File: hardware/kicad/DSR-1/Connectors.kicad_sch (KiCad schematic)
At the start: 0 parts

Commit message: Completed microcontroller schematic
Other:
- title: (none) -> Connectors
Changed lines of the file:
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@@
 	(generator_version "10.0")
 	(paper "A4")
+	(title_block
+		(title "Connectors")
+		(date "2026-05-31")
+		(rev "1")
+	)
 	(hierarchical_label "SPEED_TUNE_SW"
 		(shape output)

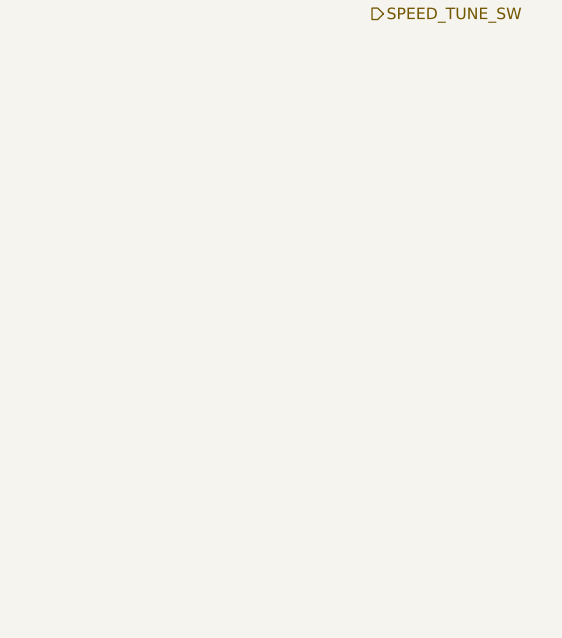
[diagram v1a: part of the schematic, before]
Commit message: completed schematics through sheet 5.
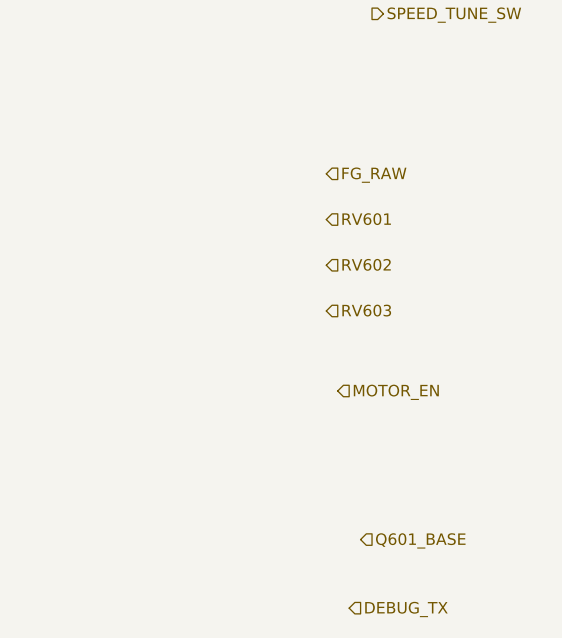
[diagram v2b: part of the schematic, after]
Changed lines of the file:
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@@
 		(rev "1")
+	)
+	(hierarchical_label "DEBUG_TX"
+		(shape input)
+		(at 262.89 99.06 0)
+		(effects
+			(font
+				(size 1.27 1.27)
+			)
+			(justify left)
+		)
 	)
 	(hierarchical_label "SPEED_TUNE_SW"
@@
 		)
 	)
+	(hierarchical_label "MOTOR_EN"
+		(shape input)
+		(at 261.62 74.93 0)
+		(effects
+			(font
+				(size 1.27 1.27)
+			)
+			(justify left)
+		)
+	)
+	(hierarchical_label "RV603"
+		(shape input)
+		(at 260.35 66.04 0)
+		(effects
+			(font
+				(size 1.27 1.27)
+			)
+			(justify left)
+		)
+	)
+	(hierarchical_label "RV601"
+		(shape input)
+		(at 260.35 55.88 0)
+		(effects
+			(font
+				(size 1.27 1.27)
+			)
+			(justify left)
+		)
+	)
+	(hierarchical_label "RV602"
+		(shape input)
+		(at 260.35 60.96 0)
+		(effects
+			(font
+				(size 1.27 1.27)
+			)
+			(justify left)
+		)
+	)
 	(hierarchical_label "SWDIO"
 		(shape output)
@@
 		(effects
 			(font
+				(size 1.27 1.27)
+			)
+			(justify left)
+		)
+	)
+	(hierarchical_label "Q601_BASE"
+		(shape input)
+		(at 264.16 91.44 0)
+		(effects
+			(font
+				(size 1.27 1.27)
+			)
+			(justify left)
+		)
+	)
+	(hierarchical_label "FG_RAW"
+		(shape input)
+		(at 260.35 50.8 0)
+		(effects
+			(font
